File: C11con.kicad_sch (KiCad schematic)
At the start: 16 parts, among them J3 Slot-0, J4 Slot-a1, J6 Screw_Terminal_01x04, J7 Slot-a0

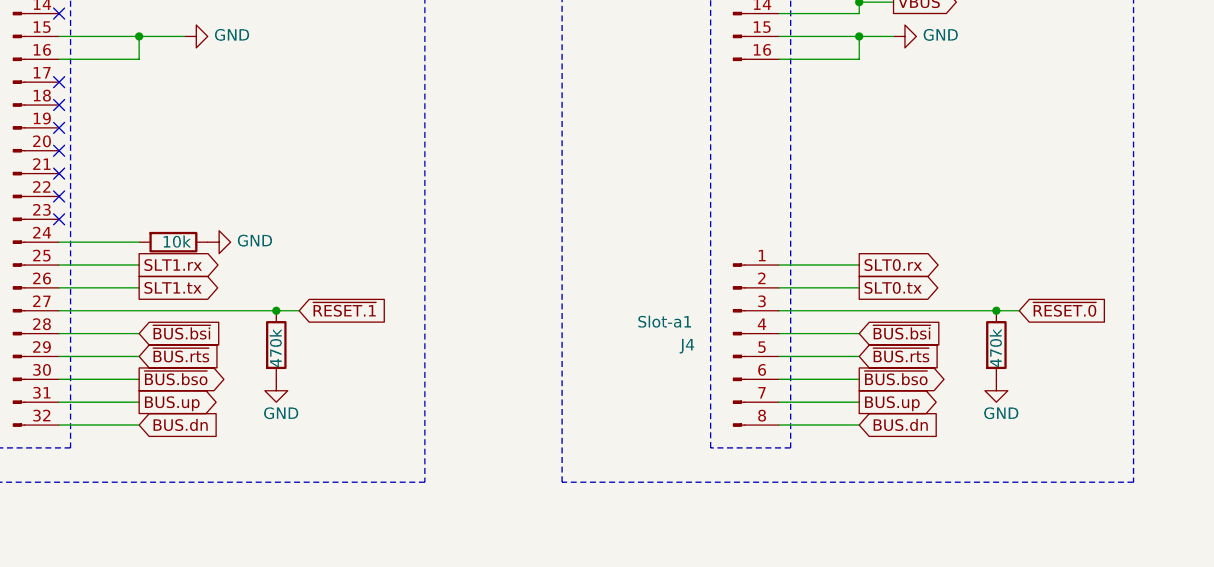
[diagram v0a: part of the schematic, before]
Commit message: mod: changed to buck converter
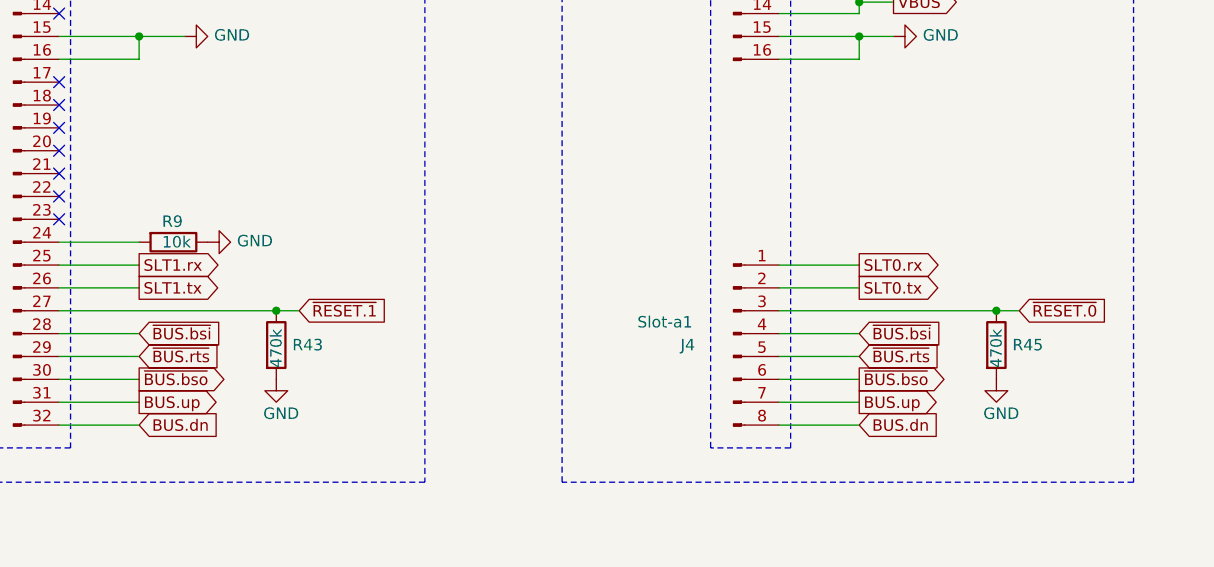
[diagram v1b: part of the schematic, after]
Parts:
- C.0, H1, H2, H3, H4, H5, H6, H8, H9, J3, J4, J6, J7: now left out of the parts list
- R43, R45: LCSC Part # (none) -> C23178
- R9: LCSC Part # (none) -> C25804
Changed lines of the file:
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@@
 		(unit 1)
 		(exclude_from_sim no)
-		(in_bom yes)
+		(in_bom no)
 		(on_board yes)
 		(dnp no)
@@
 		(unit 1)
 		(exclude_from_sim no)
-		(in_bom yes)
+		(in_bom no)
 		(on_board yes)
 		(dnp no)
@@
 		(unit 1)
 		(exclude_from_sim no)
-		(in_bom yes)
+		(in_bom no)
 		(on_board yes)
 		(dnp no)
@@
 		(unit 1)
 		(exclude_from_sim no)
-		(in_bom yes)
+		(in_bom no)
 		(on_board yes)
 		(dnp no)
@@
 		(unit 1)
 		(exclude_from_sim no)
-		(in_bom yes)
+		(in_bom no)
 		(on_board yes)
 		(dnp no)
@@
 		(unit 1)
 		(exclude_from_sim no)
-		(in_bom yes)
+		(in_bom no)
 		(on_board yes)
 		(dnp no)
@@
 		(unit 1)
 		(exclude_from_sim no)
-		(in_bom yes)
+		(in_bom no)
 		(on_board yes)
 		(dnp no)
@@
 		(unit 1)
 		(exclude_from_sim no)
-		(in_bom yes)
+		(in_bom no)
 		(on_board yes)
 		(dnp no)
@@
 		(unit 1)
 		(exclude_from_sim no)
-		(in_bom yes)
+		(in_bom no)
 		(on_board yes)
 		(dnp no)
@@
 		(unit 1)
 		(exclude_from_sim no)
-		(in_bom yes)
+		(in_bom no)
 		(on_board yes)
 		(dnp no)
@@
 		(dnp no)
 		(property "Reference" "R45"
-			(at 154.178 108.0516 0)
-			(effects
-				(font
-					(size 1.27 1.27)
-				)
-				(justify left)
-				(hide yes)
+			(at 154.178 109.22 0)
+			(effects
+				(font
+					(size 1.27 1.27)
+				)
+				(justify left)
 			)
 		)
@@
 			)
 		)
-		(property "Description" ""
+		(property "Description" "-55℃~+155℃ 100mW 470kΩ 75V Thick Film Resistor ±1% ±100ppm/℃ 0603 Chip Resistor - Surface Mount ROHS"
 			(at 152.4 109.22 0)
 			(effects
@@
 					(size 1.27 1.27)
 				)
+				(hide yes)
+			)
+		)
+		(property "LCSC Part #" "C23178"
+			(at 152.4 109.22 0)
+			(effects
+				(font
+					(size 1.27 1.27)
+				)
+				(hide yes)
 			)
 		)
@@
 		(dnp no)
 		(property "Reference" "R43"
-			(at 74.168 108.0516 0)
-			(effects
-				(font
-					(size 1.27 1.27)
-				)
-				(justify left)
-				(hide yes)
+			(at 74.168 109.22 0)
+			(effects
+				(font
+					(size 1.27 1.27)
+				)
+				(justify left)
 			)
 		)
@@
 			)
 		)
-		(property "Description" ""
+		(property "Description" "-55℃~+155℃ 100mW 470kΩ 75V Thick Film Resistor ±1% ±100ppm/℃ 0603 Chip Resistor - Surface Mount ROHS"
 			(at 72.39 109.22 0)
 			(effects
@@
 					(size 1.27 1.27)
 				)
+				(hide yes)
+			)
+		)
+		(property "LCSC Part #" "C23178"
+			(at 72.39 109.22 0)
+			(effects
+				(font
+					(size 1.27 1.27)
+				)
+				(hide yes)
 			)
 		)
@@
 		(unit 1)
 		(exclude_from_sim no)
-		(in_bom yes)
+		(in_bom no)
 		(on_board yes)
 		(dnp no)
@@
 		(unit 1)
 		(exclude_from_sim no)
-		(in_bom yes)
+		(in_bom no)
 		(on_board yes)
 		(dnp no)
@@
 		(unit 1)
 		(exclude_from_sim no)
-		(in_bom yes)
+		(in_bom no)
 		(on_board yes)
 		(dnp no)
@@
 		(dnp no)
 		(property "Reference" "R9"
-			(at 62.1284 99.568 0)
-			(effects
-				(font
-					(size 1.27 1.27)
-				)
-				(justify left)
-				(hide yes)
+			(at 59.69 95.504 90)
+			(effects
+				(font
+					(size 1.27 1.27)
+				)
+				(justify left)
 			)
 		)
@@
 			)
 		)
-		(property "Description" ""
+		(property "Description" "-55℃~+155℃ 100mW 10kΩ 75V Thick Film Resistor ±1% ±100ppm/℃ 0603 Chip Resistor - Surface Mount ROHS"
 			(at 60.96 97.79 0)
 			(effects
@@
 					(size 1.27 1.27)
 				)
-			)
-		)
+				(hide yes)
+			)
+		)
+		(property "LCSC Part #" "C25804"
+			(at 60.96 97.79 90)
+			(effects
+				(font
+					(size 1.27 1.27)
+				)
+				(hide yes)
+			)
+		)
